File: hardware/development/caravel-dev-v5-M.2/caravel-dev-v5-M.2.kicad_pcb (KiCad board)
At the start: 2 copper layers, 76.2 x 73.8 mm, 69 parts, among them J1 USB_B_Micro, J10 Conn_01x28_Pin, J11 Conn_01x28_Pin, J2 Conn_01x02_Pin, J3 Conn_01x02_Pin, J4 Conn_01x03_Pin, J5 Conn_01x02_Pin, J6 Conn_01x02_Pin, J7 Conn_01x06_Pin, J8 Conn_01x02_Pin, J9 Conn_01x02_Pin, SW1 SW_Push - SKQGADE010, T1 Logo, T2 Logo, U1 FT232H, U2 SN74LVC1G125DCKR, U3 SN74LVC1G125DCKR, U5 TAR5SxxU, U6 TAR5SxxU, U7 W25Q32FVSS, U8 M.2-CONNECTOR-E, X1 DSC6001_10MHZ, Y1 12MHz

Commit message: ~ update caravel REV5B board files
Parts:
- added TP3: TestPoint, TestPoint:TestPoint_Loop_D1.80mm_Drill1.0mm_Beaded, F.Cu at (136.2, 128.8)
- added TP4: TestPoint, TestPoint:TestPoint_Loop_D1.80mm_Drill1.0mm_Beaded, F.Cu at (136.2, 132.6)
- added TP5: TestPoint, TestPoint:TestPoint_Loop_D1.80mm_Drill1.0mm_Beaded, F.Cu at (136.2, 136.3)
- added TP6: TestPoint, TestPoint:TestPoint_Loop_D1.80mm_Drill1.0mm_Beaded, F.Cu at (136.2, 140.1)
- moved T2 18.4 mm to (137.5, 147.4)
- moved T1 18.0 mm to (137.5, 151.6)
- moved J3 3.80 mm to (150.1, 167.8), turned to 180 degrees
- moved R4 3.43 mm to (148.3, 152.3)
- moved TP1 3.04 mm to (108.2, 188.7)
- moved TP2 1.93 mm to (162.0, 189.5)
- moved R3 1.49 mm to (146.1, 149.5), turned to -90 degrees
- moved C8 0.67 mm to (145.0, 143.4)
- moved R11 0.56 mm to (161.6, 128.8)
- moved Y1 0.17 mm to (158.2, 130.1)
- moved D3 0.11 mm to (162.7, 134.4)
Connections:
- J10 pad 1: /mprj_io[37] -> /ACBUS1
- J10 pad 2: /mprj_io[36] -> GND
- J10 pad 3: /mprj_io[35] -> +3V3
- J10 pad 4: /mprj_io[34] -> /mprj_io[37]
- J10 pad 5: /ACBUS1 -> /mprj_io[36]
- J10 pad 6: GND -> /mprj_io[35]
- J10 pad 7: +3V3 -> /mprj_io[34]
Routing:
- net +3V3: track 382.4 -> 402.7 mm
- net /ADBUS4: track 0.00 -> 16.9 mm
- net /ADBUS5: track 0.00 -> 13.7 mm
- net /ADBUS6: track 0.00 -> 12.3 mm
- net /ADBUS7: track 0.00 -> 11.9 mm
- net /mprj_io[34]: track 60.5 -> 52.3 mm
- net /mprj_io[37]: track 68.4 -> 60.3 mm
- net /mprj_io[36]: track 65.8 -> 57.7 mm
- net /mprj_io[35]: track 62.6 -> 54.6 mm
- net GND: track 82.9 -> 79.2 mm, vias 29 -> 28
- net +1V8: track 243.2 -> 245.2 mm
- net Net-(D2-A): track 5.97 -> 4.64 mm
- net /ACBUS0: track 43.7 -> 44.9 mm
- net /USB_SI: track 94.2 -> 95.4 mm
- net /USB_CS1: track 95.2 -> 96.2 mm
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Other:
- board text added: "ADBUS4"
- board text added: "ADBUS5"
- board text added: "ADBUS6"
- board text added: "ADBUS7"
- board text added: "~{CS}"
- board text removed: "CS"

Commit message: ~ update caravel REV5B
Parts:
- removed TP3, TP4, TP5, TP6: TestPoint, TestPoint:TestPoint_Loop_D1.80mm_Drill1.0mm_Beaded
- added J12: Conn_01x04_Pin, Connector_PinHeader_2.54mm:PinHeader_1x04_P2.54mm_Vertical, F.Cu at (136.9, 130.2)
- moved T2 5.90 mm to (133.4, 143.1)
- moved T1 5.80 mm to (133.3, 147.6)
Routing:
- net /ADBUS4: track 16.9 -> 15.6 mm
- net /ADBUS5: track 13.7 -> 13.0 mm
- net +3V3: track 402.7 -> 403.3 mm
- net /ADBUS7: track 11.9 -> 11.3 mm
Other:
- board text added: "OSC ~{EN}"
- board text added: "UART ~{EN}"
- board text removed: "OSC EN"

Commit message: ~ update caravel REV 5B PCB
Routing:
- net /ACBUS1: track 126.3 -> 129.3 mm

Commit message: ~ update caravel REV 5B PCB
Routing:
- net /ACBUS1: track 129.3 -> 128.8 mm

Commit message: ~ enhance caravel REV 5B power tracks
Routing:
- net +3V3: track 403.3 -> 385.0 mm
- net +1V8: track 245.2 -> 243.7 mm

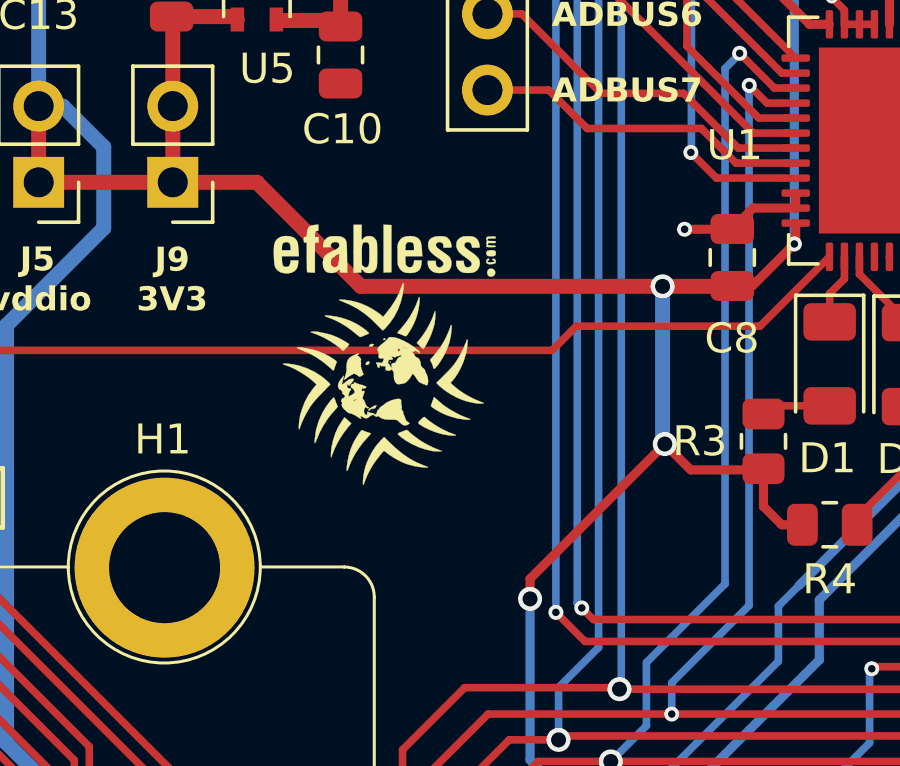
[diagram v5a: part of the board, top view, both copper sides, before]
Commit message: ~ update caravel REV 5B with larger logos
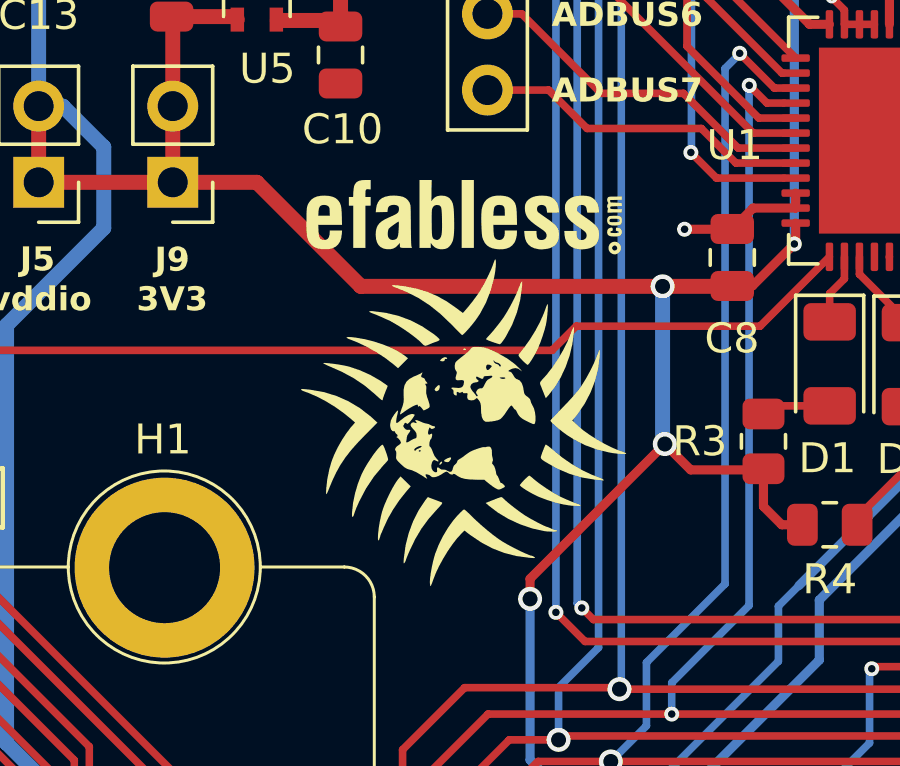
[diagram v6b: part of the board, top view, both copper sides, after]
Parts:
- T1: footprint Caravel_Board:logo -> Caravel_Board:logo_large
- T2: footprint Caravel_Board:ef_logo -> Caravel_Board:ef_logo_large
- moved T1 2.93 mm to (136.0, 148.8)
- moved T2 2.84 mm to (136.0, 142.0)

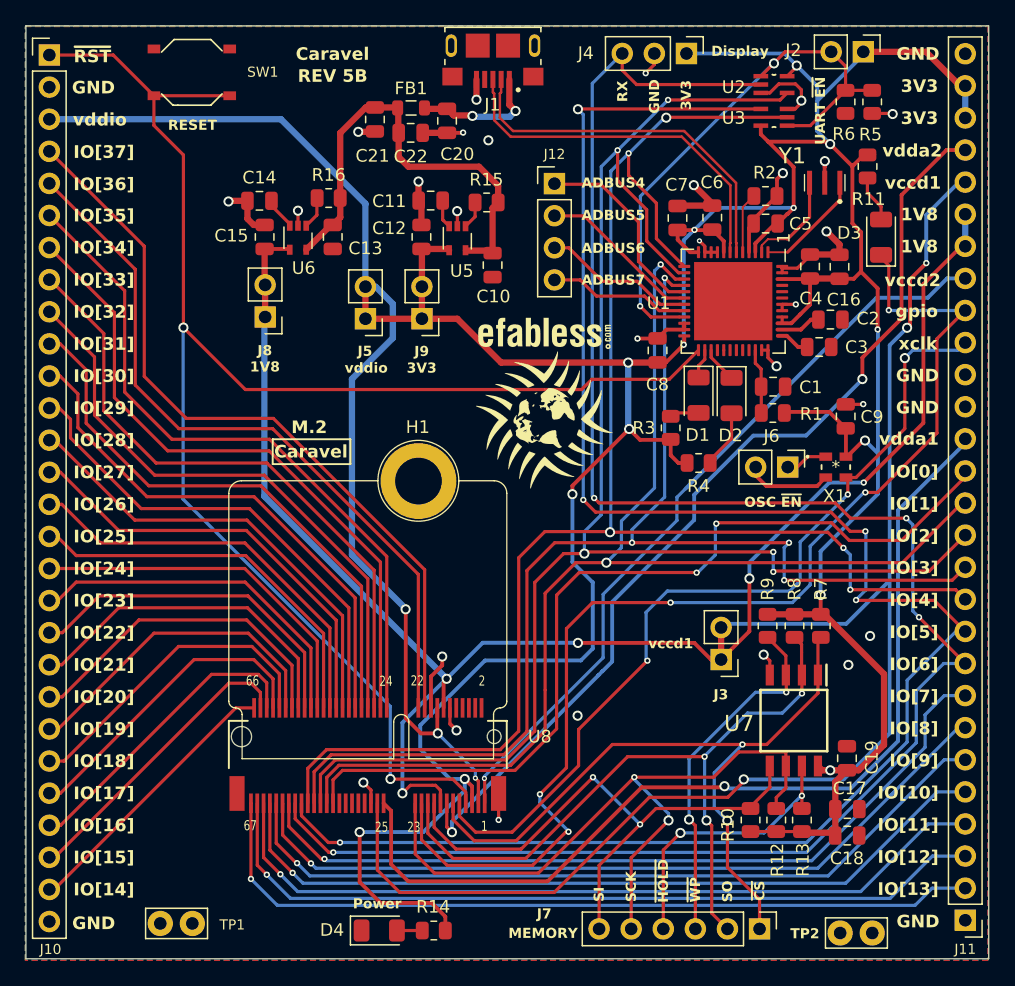
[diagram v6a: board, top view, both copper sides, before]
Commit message: ~ update caravel REV 5B logos
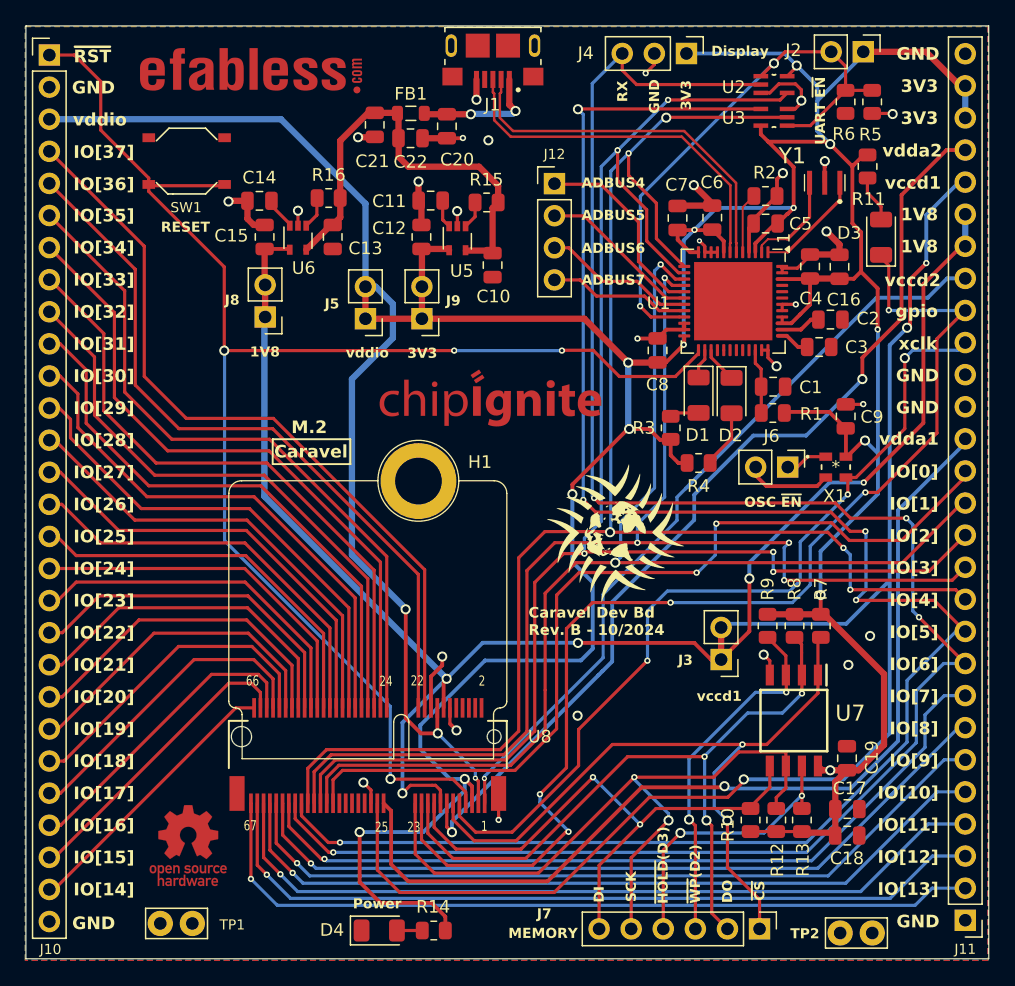
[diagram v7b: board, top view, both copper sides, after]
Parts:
- added T3: oshw logo CU, Caravel_Board:oshw-logo, F.Cu at (107.9, 182.6)
- added T4: ci logo CU, Caravel_Board:chipIgnite_logo, F.Cu at (139.2, 146.5)
- T1: value Logo -> ef world logo
- T2: value Logo -> ef logo CU; footprint Caravel_Board:ef_logo_large -> Caravel_Board:ef_logo-cu
- moved T2 33.9 mm to (110.1, 120.2)
- moved T1 10.6 mm to (141.6, 157.8)
- moved SW1 7.03 mm to (107.8, 128.4)
- moved C20 0.43 mm to (128.3, 125.6)
- moved C21 0.43 mm to (122.6, 125.5)
- moved C22 0.43 mm to (125.5, 126.6)
- moved FB1 0.43 mm to (125.5, 124.6)
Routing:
- net /ACBUS1: track 128.8 -> 122.2 mm, vias 2 -> 4
- net +5V: track 36.3 -> 35.5 mm
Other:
- board text added: "Caravel Dev Bd Rev. B - 10/2024"
- board text added: "DI"
- board text added: "DO"
- board text added: "~{HOLD}(D3)"
- board text added: "~{WP}(D2)"
- board text removed: "REV 5B"
- board text removed: "SI"
- board text removed: "SO"
- board text removed: "~{HOLD}"
- board text removed: "~{WP}"
